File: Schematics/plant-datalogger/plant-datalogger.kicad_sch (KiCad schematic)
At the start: 3 parts, among them U1 PicoW

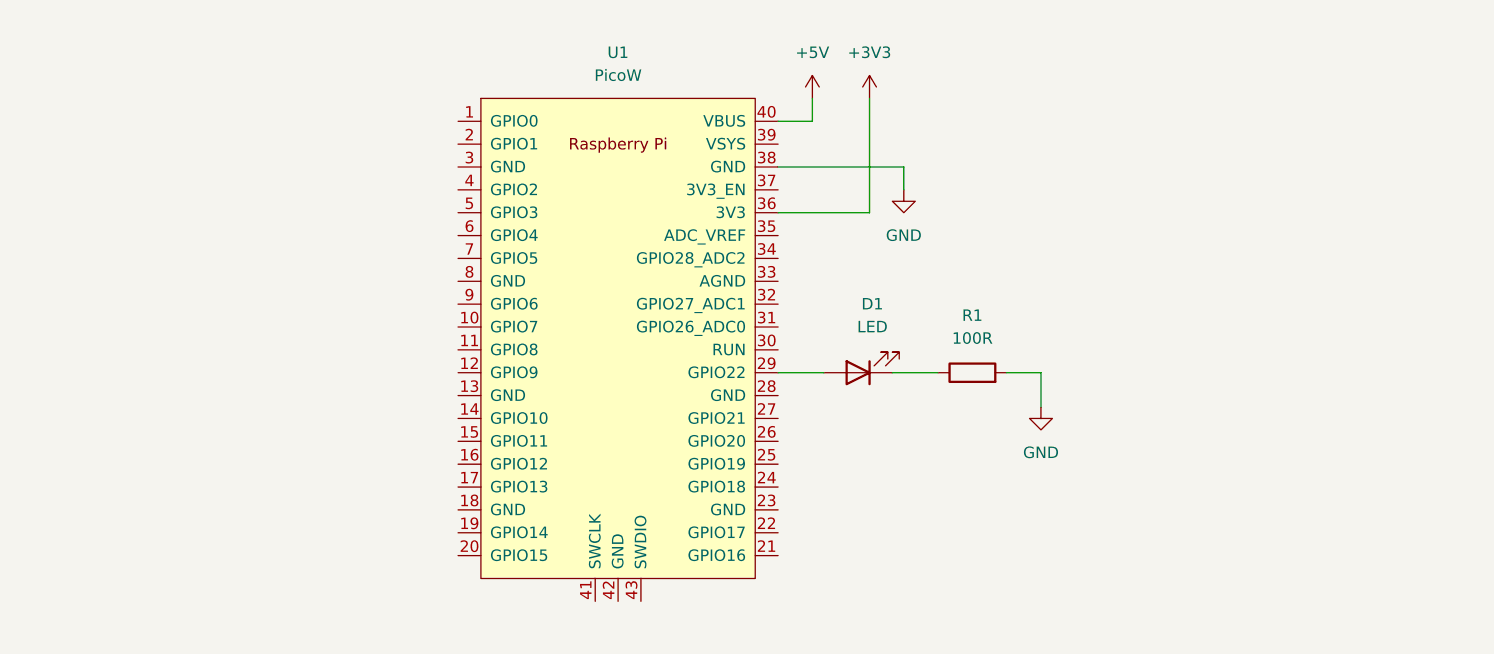
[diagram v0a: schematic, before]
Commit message: Updated project schematic output for markdown embedding
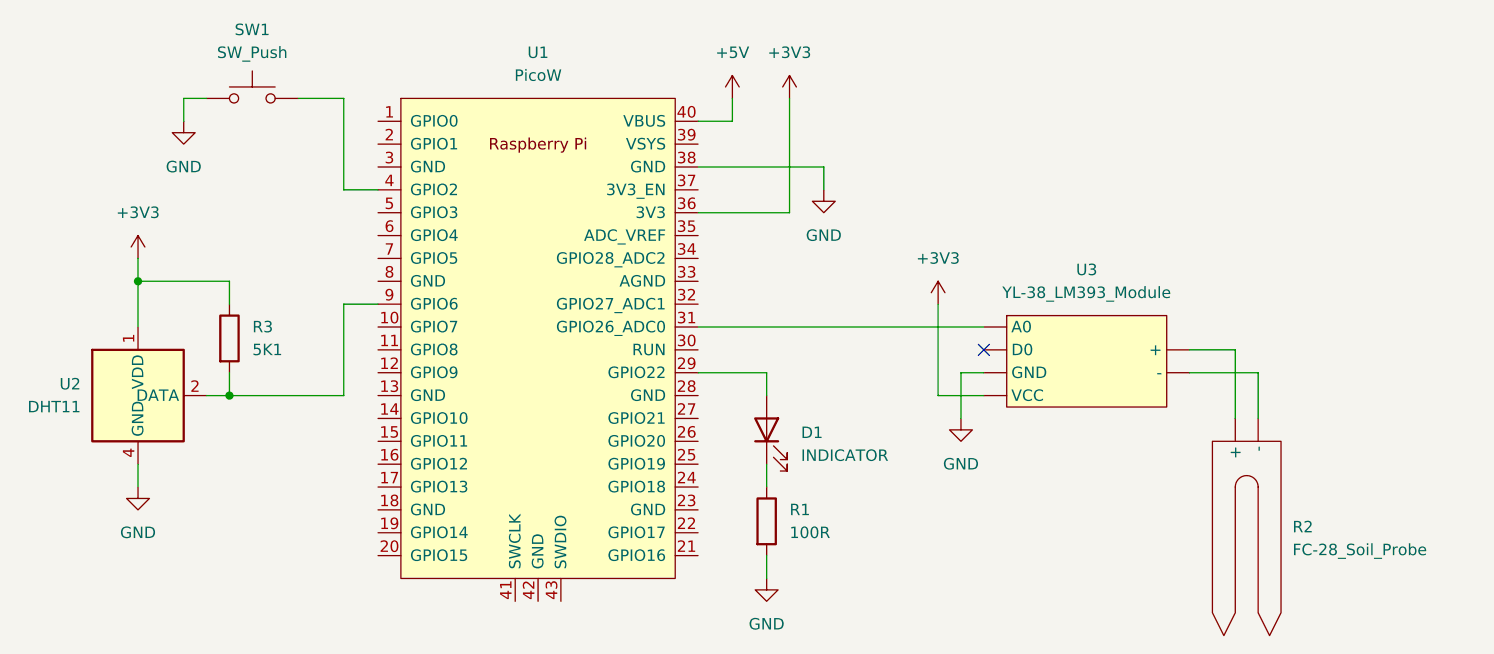
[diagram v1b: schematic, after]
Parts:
- added R2: FC-28_Soil_Probe, symbol rbe200x:FC-28_Soil_Probe
- added R3: 5K1, symbol Device:R
- added SW1: SW_Push, symbol Switch:SW_Push
- added U2: DHT11, Sensor:Aosong_DHT11_5.5x12.0_P2.54mm, symbol Sensor:DHT11
- added U3: YL-38_LM393_Module, symbol rbe200x:YL-38_LM393_Module
- D1: value LED -> INDICATOR
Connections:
- net +3V3: now also R3.1, U2.1 (VDD), U3. (VCC)
- net GND: now also SW1.1, U2.4 (GND), U3. (VCC)
- net at U1.31 (GPIO26_ADC0): now also U3. (VCC)
- net at U1.4 (GPIO2): now also SW1.2
- net at U1.9 (GPIO6): now also R3.2, U2.2 (DATA)
- new net: R2. (-), U3. (VCC) (x2)
- no-connect marks 0 -> 1
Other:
- moved on the sheet: D1, R1, U1
